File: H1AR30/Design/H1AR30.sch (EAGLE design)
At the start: 21 parts, among them P1 HEXABIT_17.32_NO_P3, U1 STM32F091CBU6, X1 XTALL_CSTCE8M00G52

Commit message: in this commit: - schematic is done - PCB is done - all output files were generated
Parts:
- added C10: 4.7uF, Hexabitz:C-0805-POL
- added C11, C12, C15: 100nF, Hexabitz:C-0603
- added C13, C14: 47pF, Hexabitz:C-0603
- added C16: 100uF, Hexabitz:C-3225TDK_C3225X5R0J107M250AC_0_0
- added C17: 1uF, Hexabitz:C-0805-POL
- added D2: RED, Hexabitz:VLMS1300-GS08
- added D3: GREEN, Hexabitz:VLMTG1300-GS08
- added FB2: (no value), Hexabitz:FB-TDK_MMZ1608Y300B
- added PWR: 3-644456-2, Hexabitz:3-644456-2
- added R4, R5: 27.0Ω, Hexabitz:R-0603
- added R6: 39.0Ω, Hexabitz:R-0603
- added R7: 270.0Ω, Hexabitz:R-0603
- added R8: 4.7kΩ, Hexabitz:R-0603
- added R9: 10kΩ, Hexabitz:R-0603
- added U2: FT230XQ-R, Hexabitz:FT230XQ-R
- added U3: LM3940IMP-3.3, Hexabitz:LM3940IMP-3.3
- added USB-B*: 1981568-1, Hexabitz:1981568-1
- C1: value 10nF -> 100nF; CAPACITANCE 10nF -> 100nF; MPN C0603C103K5RACTU -> C0603C104K8RACTU; OCTOPART_URL https://octopart.com/c0603c103k5ractu-kemet-133094?r=sp&s=R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 -> https://octopart.com/c0603c104k8ractu-kemet-145075?r=sp&s=9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; VOLTAGE_RATING 50V -> 10V
- C3: value 100nF -> 4.7uF; device Hexabitz:C-0603 -> Hexabitz:C-0805-POL; CAPACITANCE 100nF -> 4.7uF; MFN KEMET -> Murata; MPN C0603C104K8RACTU -> GRM21BC81E475KA12L; OCTOPART_URL https://octopart.com/c0603c104k8ractu-kemet-145075?r=sp&s=9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 -> https://octopart.com/grm21bc81e475ka12l-murata-10331911?r=s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; VOLTAGE_RATING 10V -> 25V
- C5: value 100nF -> 10nF; CAPACITANCE 100nF -> 10nF; MPN C0603C104K8RACTU -> C0603C103K5RACTU; OCTOPART_URL https://octopart.com/c0603c104k8ractu-kemet-145075?r=sp&s=9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 -> https://octopart.com/c0603c103k5ractu-kemet-133094?r=sp&s=R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; VOLTAGE_RATING 10 -> 50V
- C7: value 4.7uF -> 100nF; device Hexabitz:C-0805-POL -> Hexabitz:C-0603; CAPACITANCE 4.7uF -> 100nF; MFN Murata -> KEMET; MPN GRM21BC81E475KA12L -> C0603C104K8RACTU; OCTOPART_URL https://octopart.com/grm21bc81e475ka12l-murata-10331911?r=s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 -> https://octopart.com/c0603c104k8ractu-kemet-145075?r=sp&s=9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; VOLTAGE_RATING 25V -> 10
- D1: value VLMS1300-GS08 -> RED
- R2: value 0.0R -> 10.0K; MFN Yageo -> Vishay; MPN RC0603JR-070RL -> CRCW060310K0JNEB; OCTOPART_URL https://octopart.com/rc0603jr-070rl-yageo-1241539?r=sp&s=X2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 -> https://octopart.com/crcw060310k0jneb-vishay+dale-46603268; RESISTANCE 0.0 Ohm -> 10.0K Ohm; TOLERANCE (none) -> 5%
- R3: value 10.0K -> 0.0R; MPN RC0603JR-0710KL -> RC0603JR-070RL; OCTOPART_URL https://octopart.com/search?q=RC0603JR-0710KL&start=0 -> https://octopart.com/rc0603jr-070rl-yageo-1241539?r=sp&s=X2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; RESISTANCE 10.0K Ohm -> 0.0 Ohm; TOLERANCE 5% -> (none)
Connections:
- new net N$1: R1.2, U1.PA6
- new net N$10: FB2.2, PWR.2
- new net N$11: C17.+, FB2.1, U3.IN
- new net N$12: R5.2, U2.USBDP
- new net N$13: R4.2, U2.USBDM
- new net N$14: R7.1, U2.CBUS2
- new net N$15: R6.1, U2.CBUS1
- new net N$16: D2.C, R7.2
- new net N$17: D3.C, R6.2
- new net N$18: PWR.1, R8.2, USB-B*.1
- new net N$2: C14.1, R4.1, USB-B*.2
- new net UART1_CTS: U1.PA11, U2.!RTS!
- new net UART1_RTS: U1.PA12, U2.!CTS!
- new net VBUS_SENSE: R8.1, R9.2, U2.CBUS3
- net B1: now also R2.2; no longer R3.2
- net GND: now also C1.2, C10.-, C11.2, C12.2, C13.2, C14.2, C15.2, C16.1, C17.-, C3.-, C7.2, R9.1, U1.PA15, U1.PB1, U1.PB14, U1.PC14-OSC32_IN, U2.GND@13, U2.GND@17, U2.GND@3, U3.GND, U3.GND_2, USB-B*.5, USB-B*.SHIELD; no longer C3.2, C5.2, C7.-
- net N$3: now also C13.1, R5.1, USB-B*.3; no longer R1.2, U1.PA11
- net R1: now also C1.1; no longer C8.1
- net UART1_RX: now also U2.TXD
- net UART1_TX: now also U2.RXD
- net UART2_RX: now also P1.SD1
- net UART2_TX: now also P1.SU1
- net UART3_RX: now also P1.SD4
- net UART3_TX: now also P1.SU4
- net UART4_RX: now also P1.SD5
- net UART4_TX: now also P1.SU5
- net UART5_RX: now also P1.SD6
- net UART5_TX: now also P1.SU6
- net UART6_RX: now also P1.SD2
- net UART6_TX: now also P1.SU2
- net VDD: now also C10.+, C11.1, C12.1, C15.1, C16.2, C3.+, C7.1, C8.1, D2.A, D3.A, U2.!RESET!, U2.3V3OUT, U2.VCC, U2.VCCIO, U3.OUT; no longer C3.1, C5.1, C7.+
- net VDDA: now also C5.1; no longer C1.1
- net VSSA: now also C5.2, R3.2; no longer C1.2, R2.2
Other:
- note added: "Anas Kaadan"
- note added: "MICRO USB-B TO UART CONVERTER"
- note added: "VDD = 3.3v"
- note removed: "Add Description Here"
- moved on the sheet: C, C1, C4, C5, C6, C8, D, D1, R1, R2, R3

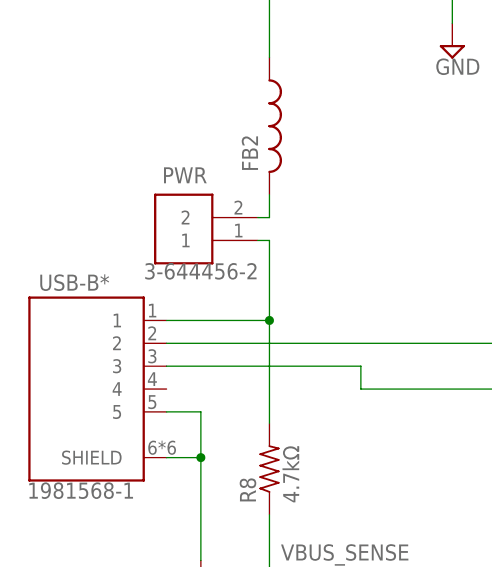
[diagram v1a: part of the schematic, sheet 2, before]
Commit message: replaced (USB-B*) with (PUSB*) and fixed gerber files
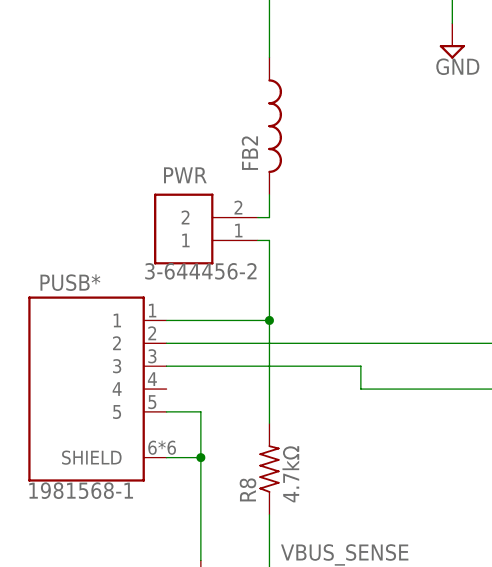
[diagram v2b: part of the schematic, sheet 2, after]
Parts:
- renumbered USB-B* to PUSB*
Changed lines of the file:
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@@
 <part name="GND10" library="supply1" library_urn="urn:adsk.eagle:library:371" deviceset="GND" device=""/>
 <part name="GND11" library="supply1" library_urn="urn:adsk.eagle:library:371" deviceset="GND" device=""/>
-<part name="USB-B*" library="Hexabitz" deviceset="1981568-1" device=""/>
+<part name="PUSB*" library="Hexabitz" deviceset="1981568-1" device=""/>
 </parts>
 <sheets>
@@
 <attribute name="VALUE" x="79.8063" y="152.4478" size="2.08318125" layer="96" ratio="10" rot="SR0"/>
 </instance>
-<instance part="USB-B*" gate="G$1" x="31.75" y="114.3" smashed="yes">
+<instance part="PUSB*" gate="G$1" x="31.75" y="114.3" smashed="yes">
 <attribute name="NAME" x="25.14168125" y="125.2308" size="1.779440625" layer="95"/>
 <attribute name="VALUE" x="23.8708" y="103.8981" size="1.77973125" layer="96" rot="MR180"/>
@@
 <wire x1="43.18" y1="106.68" x2="43.18" y2="111.76" width="0.1524" layer="91"/>
 <wire x1="43.18" y1="111.76" x2="39.37" y2="111.76" width="0.1524" layer="91"/>
-<pinref part="USB-B*" gate="G$1" pin="5"/>
-<pinref part="USB-B*" gate="G$1" pin="SHIELD"/>
+<pinref part="PUSB*" gate="G$1" pin="5"/>
+<pinref part="PUSB*" gate="G$1" pin="SHIELD"/>
 <wire x1="39.37" y1="106.68" x2="43.18" y2="106.68" width="0.1524" layer="91"/>
 <junction x="43.18" y="106.68"/>
@@
 <wire x1="114.3" y1="119.38" x2="92.71" y2="119.38" width="0.1524" layer="91"/>
 <junction x="92.71" y="119.38"/>
-<pinref part="USB-B*" gate="G$1" pin="2"/>
+<pinref part="PUSB*" gate="G$1" pin="2"/>
 </segment>
 </net>
@@
 <wire x1="60.96" y1="114.3" x2="80.01" y2="114.3" width="0.1524" layer="91"/>
 <junction x="80.01" y="114.3"/>
-<pinref part="USB-B*" gate="G$1" pin="3"/>
+<pinref part="PUSB*" gate="G$1" pin="3"/>
 </segment>
 </net>
@@
 <pinref part="PWR" gate="G$1" pin="1"/>
 <wire x1="49.53" y1="130.81" x2="50.8" y2="130.81" width="0.1524" layer="91"/>
-<pinref part="USB-B*" gate="G$1" pin="1"/>
+<pinref part="PUSB*" gate="G$1" pin="1"/>
 </segment>
 </net>

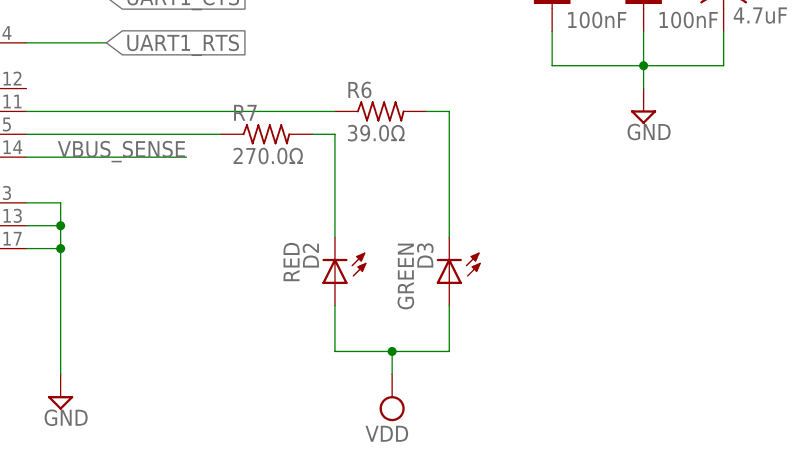
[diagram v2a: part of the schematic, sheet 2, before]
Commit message: changed LED's colors, updated BOM and PDF schematic
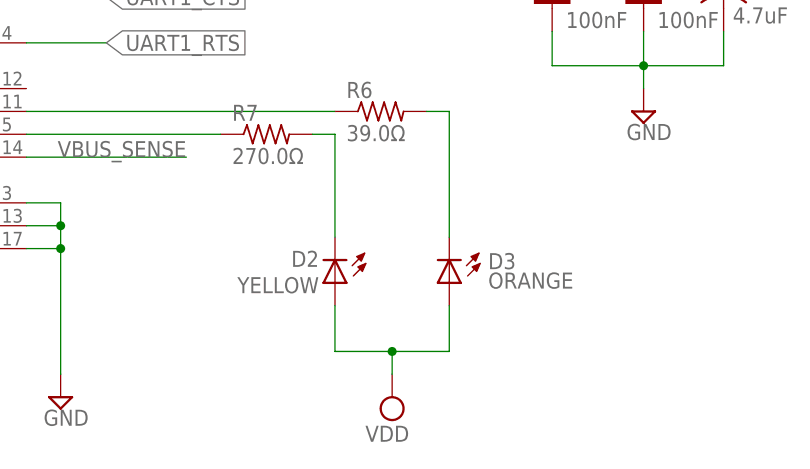
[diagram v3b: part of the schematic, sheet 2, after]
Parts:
- D2: value RED -> YELLOW; MPN (none) -> VLMY1300-GS08; OCTOPART_URL (none) -> https://octopart.com/vlmy1300-gs08-vishay-21709204?r=sp
- D3: value GREEN -> ORANGE; MPN (none) -> VLMO1300-GS08; OCTOPART_URL (none) -> https://octopart.com/vlmo1300-gs08-vishay-21709200?r=sp#
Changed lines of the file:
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@@
 <attribute name="TOLERANCE" value="±5%"/>
 </part>
-<part name="D2" library="Hexabitz" deviceset="VLMS1300-GS08" device="" value="RED"/>
-<part name="D3" library="Hexabitz" deviceset="VLMTG1300-GS08" device="" value="GREEN"/>
+<part name="D2" library="Hexabitz" deviceset="VLMS1300-GS08" device="" value="YELLOW">
+<attribute name="MPN" value="VLMY1300-GS08"/>
+<attribute name="OCTOPART_URL" value="https://octopart.com/vlmy1300-gs08-vishay-21709204?r=sp"/>
+</part>
+<part name="D3" library="Hexabitz" deviceset="VLMTG1300-GS08" device="" value="ORANGE">
+<attribute name="MPN" value="VLMO1300-GS08 "/>
+<attribute name="OCTOPART_URL" value="https://octopart.com/vlmo1300-gs08-vishay-21709200?r=sp#"/>
+</part>
 <part name="SUPPLY25" library="supply2" library_urn="urn:adsk.eagle:library:372" deviceset="VDD" device=""/>
 <part name="SUPPLY26" library="supply2" library_urn="urn:adsk.eagle:library:372" deviceset="GND" device=""/>
@@
 </instance>
 <instance part="D2" gate="G$1" x="215.9" y="82.55" smashed="yes" rot="R270">
-<attribute name="NAME" x="212.344" y="87.122" size="1.778" layer="95" rot="R270"/>
-<attribute name="VALUE" x="210.185" y="87.122" size="1.778" layer="96" rot="R270"/>
+<attribute name="NAME" x="214.122" y="86.106" size="1.778" layer="95" rot="R180"/>
+<attribute name="VALUE" x="214.122" y="83.185" size="1.778" layer="96" rot="R180"/>
 </instance>
 <instance part="D3" gate="G$1" x="228.6" y="82.55" smashed="yes" rot="R270">
-<attribute name="NAME" x="225.044" y="87.122" size="1.778" layer="95" rot="R270"/>
-<attribute name="VALUE" x="222.885" y="87.122" size="1.778" layer="96" rot="R270"/>
+<attribute name="NAME" x="232.918" y="84.074" size="1.778" layer="95"/>
+<attribute name="VALUE" x="232.918" y="81.915" size="1.778" layer="96"/>
 </instance>
 <instance part="SUPPLY25" gate="G$1" x="222.25" y="69.85" smashed="yes" rot="R180">
